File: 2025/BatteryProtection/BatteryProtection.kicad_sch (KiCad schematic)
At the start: 49 parts, among them J1 Conn_01x02_Socket, J2 Conn_01x02_Pin, J3 Conn_01x02_Pin, Q1 IXTA140P05T, Q10 BC847, Q11 BC847, Q12 BC847, Q2 BC847, Q3 BC847, Q4 BC847, Q5 BC847, Q6 BC847, Q7 BC847, Q8 BC847, Q9 BC847, U1 MCP6561-OT, U3 MCP6561-OT, U4 MCP1799x-330xxTT

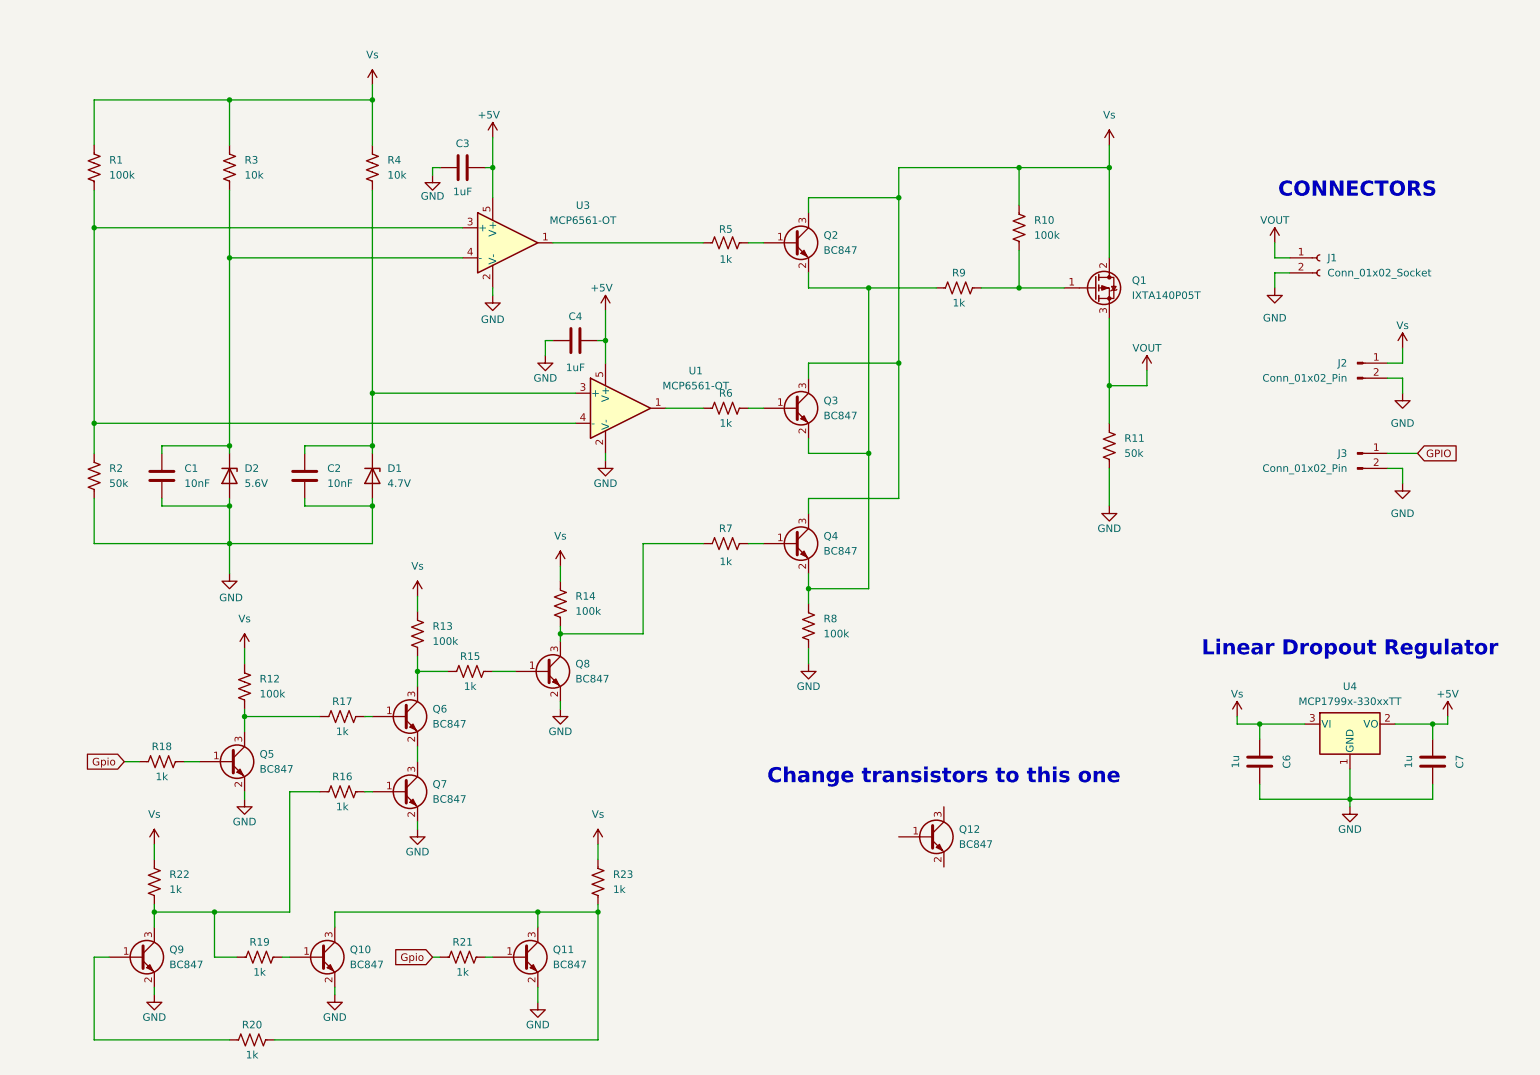
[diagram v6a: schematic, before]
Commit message: updated small bits in LTS and Kicad schematics
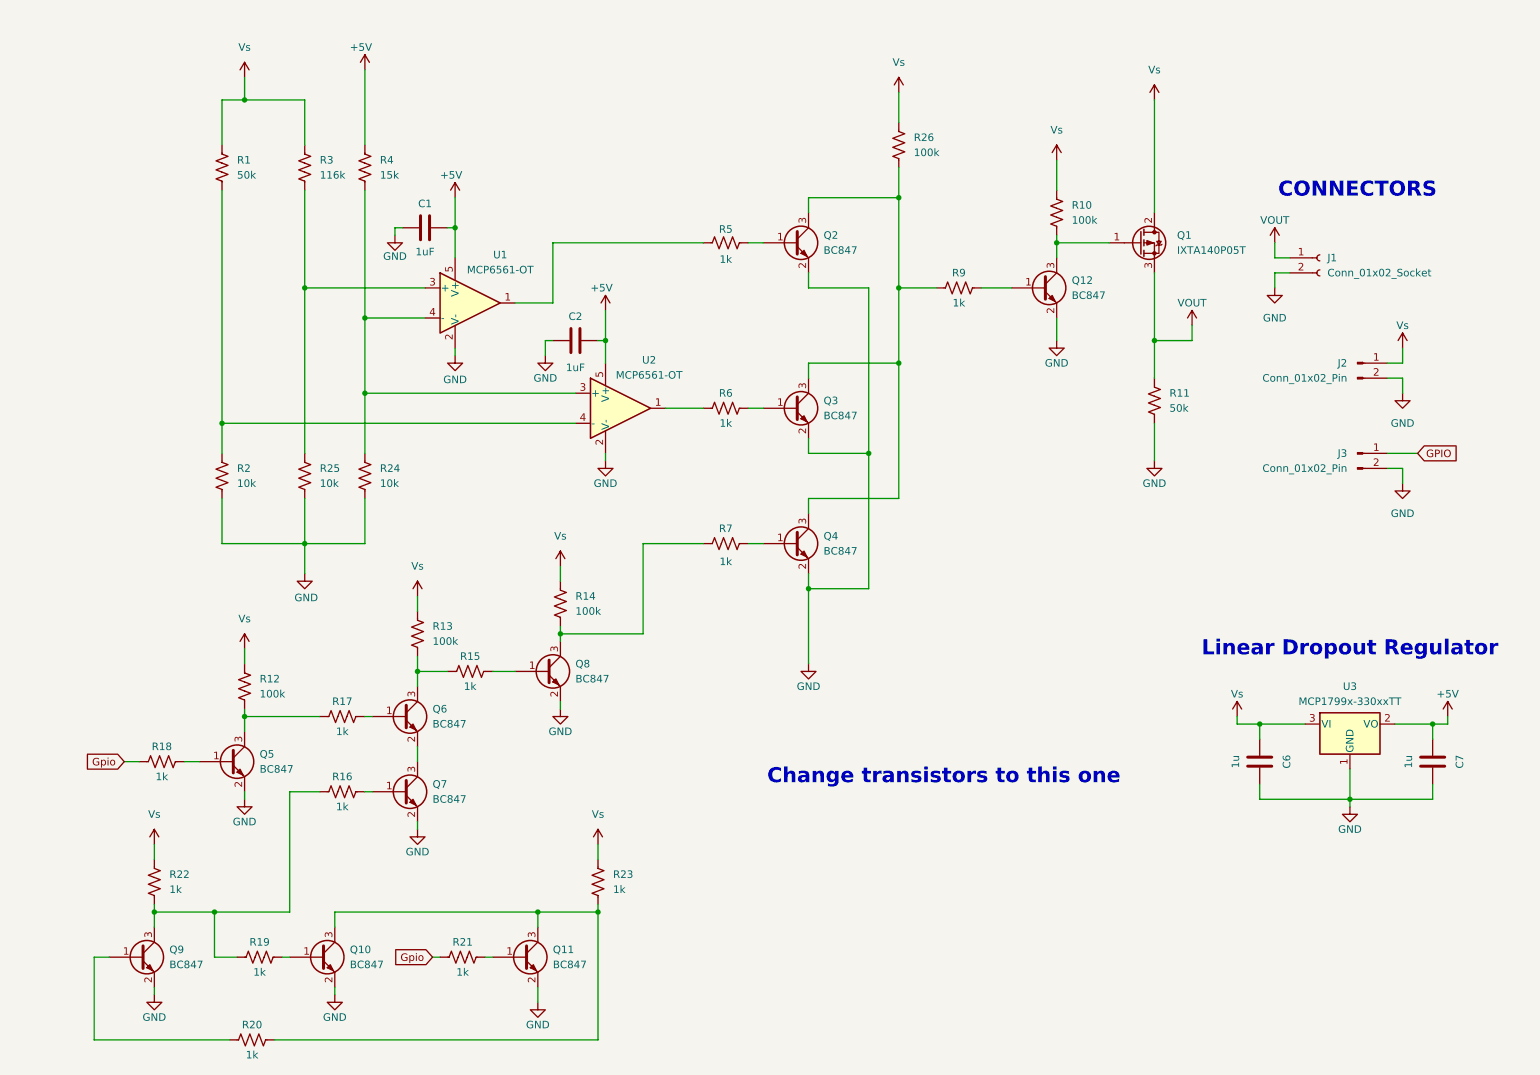
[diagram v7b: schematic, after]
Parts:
- removed C1, C2: 10nF, Capacitor_SMD:C_0603_1608Metric_Pad1.08x0.95mm_HandSolder, symbol Device:C
- removed D1: 4.7V, Diode_SMD:D_0603_1608Metric_Pad1.05x0.95mm_HandSolder, symbol Device:D_Zener
- removed D2: 5.6V, Diode_SMD:D_0603_1608Metric_Pad1.05x0.95mm_HandSolder, symbol Device:D_Zener
- removed R8: 100k, Resistor_SMD:R_0603_1608Metric_Pad0.98x0.95mm_HandSolder, symbol Device:R_US
- added R24, R25: 10k, Resistor_SMD:R_0603_1608Metric_Pad0.98x0.95mm_HandSolder, symbol Device:R_US
- added R26: 100k, Resistor_SMD:R_0603_1608Metric_Pad0.98x0.95mm_HandSolder, symbol Device:R_US
- R1: value 100k -> 50k
- R2: value 50k -> 10k
- R3: value 10k -> 116k
- R4: value 10k -> 15k
- renumbered C3 to C1, C4 to C2, U3 to U1, U1 to U2, U4 to U3
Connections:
- net +5V: now also R4.1
- net GND: now also Q12.2 (E), Q2.2 (E), Q3.2 (E), Q4.2 (E), R24.2, R25.2
- net Vs: now also R26.2; no longer Q2.3 (C), Q3.3 (C), Q4.3 (C), R4.1
- net at Q1.1 (G), R10.1: now also Q12.3 (C); no longer R9.1
- net at R4.2, U2.3 (+): now also U1.4 (-), R24.1
- net at R3.2: now also U1.3 (+), R25.1; no longer U1.4 (-)
- net at Q12.1 (B): now also R9.1
- net at R1.2, R2.1, U2.4 (-): no longer U1.3 (+)
- new net: Q2.3 (C), Q3.3 (C), Q4.3 (C), R26.1, R9.2
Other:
- moved on the sheet: C1, Q1, Q12, R1, R10, R11, R2, R3, R4, U1

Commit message: started PCB layout
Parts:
- renumbered C6 to C3, C7 to C4, R11 to R10, R12 to R11, R13 to R12, R14 to R13, R15 to R14, R18 to R15, R17 to R16, R16 to R17, R19 to R18, R20 to R19, R21 to R20, R22 to R21, R23 to R22, R24 to R23, R25 to R24, R26 to R25, R9 to R8, R10 to R9
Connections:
- net Gpio is gone; now on net GPIO: R15.1, R20.1
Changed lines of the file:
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@@
 		)
 	)
-	(global_label "Gpio"
+	(global_label "GPIO"
 		(shape input)
 		(at 44.45 142.24 180)
@@
 		)
 		(property "Intersheetrefs" "${INTERSHEET_REFS}"
-			(at 37.292 142.24 0)
+			(at 36.9895 142.24 0)
 			(effects
 				(font
@@
 		)
 	)
-	(global_label "Gpio"
+	(global_label "GPIO"
 		(shape input)
 		(at 96.52 175.26 180)
@@
 		)
 		(property "Intersheetrefs" "${INTERSHEET_REFS}"
-			(at 89.362 175.26 0)
+			(at 89.0595 175.26 0)
 			(effects
 				(font
@@
 		(dnp no)
 		(fields_autoplaced yes)
-		(property "Reference" "R22"
+		(property "Reference" "R21"
 			(at 52.07 161.2899 0)
 			(effects
@@
 			(project "BatteryProtection"
 				(path "/6c304649-7c80-4a4c-b925-07b9210ad53d"
-					(reference "R22")
+					(reference "R21")
 					(unit 1)
 				)
@@
 		(on_board yes)
 		(dnp no)
-		(property "Reference" "R19"
+		(property "Reference" "R18"
 			(at 67.31 172.72 90)
 			(effects
@@
 			(project "BatteryProtection"
 				(path "/6c304649-7c80-4a4c-b925-07b9210ad53d"
-					(reference "R19")
+					(reference "R18")
 					(unit 1)
 				)
@@
 		(dnp no)
 		(fields_autoplaced yes)
-		(property "Reference" "R12"
+		(property "Reference" "R11"
 			(at 67.31 128.2699 0)
 			(effects
@@
 			(project "BatteryProtection"
 				(path "/6c304649-7c80-4a4c-b925-07b9210ad53d"
-					(reference "R12")
+					(reference "R11")
 					(unit 1)
 				)
@@
 		(on_board yes)
 		(dnp no)
-		(property "Reference" "R21"
+		(property "Reference" "R20"
 			(at 101.6 172.72 90)
 			(effects
@@
 			(project "BatteryProtection"
 				(path "/6c304649-7c80-4a4c-b925-07b9210ad53d"
-					(reference "R21")
+					(reference "R20")
 					(unit 1)
 				)
@@
 		(dnp no)
 		(fields_autoplaced yes)
-		(property "Reference" "R10"
+		(property "Reference" "R9"
 			(at 204.47 48.2599 0)
 			(effects
@@
 			(project "BatteryProtection"
 				(path "/6c304649-7c80-4a4c-b925-07b9210ad53d"
-					(reference "R10")
+					(reference "R9")
 					(unit 1)
 				)
@@
 		(on_board yes)
 		(dnp no)
-		(property "Reference" "R20"
+		(property "Reference" "R19"
 			(at 66.04 186.69 90)
 			(effects
@@
 			(project "BatteryProtection"
 				(path "/6c304649-7c80-4a4c-b925-07b9210ad53d"
-					(reference "R20")
+					(reference "R19")
 					(unit 1)
 				)
@@
 		(dnp no)
 		(fields_autoplaced yes)
-		(property "Reference" "R26"
+		(property "Reference" "R25"
 			(at 177.8 36.8299 0)
 			(effects
@@
 			(project "BatteryProtection"
 				(path "/6c304649-7c80-4a4c-b925-07b9210ad53d"
-					(reference "R26")
+					(reference "R25")
 					(unit 1)
 				)
@@
 		(dnp no)
 		(fields_autoplaced yes)
-		(property "Reference" "R25"
+		(property "Reference" "R24"
 			(at 77.47 92.7099 0)
 			(effects
@@
 			(project "BatteryProtection"
 				(path "/6c304649-7c80-4a4c-b925-07b9210ad53d"
-					(reference "R25")
+					(reference "R24")
 					(unit 1)
 				)
@@
 		(dnp no)
 		(fields_autoplaced yes)
-		(property "Reference" "R24"
+		(property "Reference" "R23"
 			(at 87.63 92.7099 0)
 			(effects
@@
 			(project "BatteryProtection"
 				(path "/6c304649-7c80-4a4c-b925-07b9210ad53d"
-					(reference "R24")
+					(reference "R23")
 					(unit 1)
 				)
@@
 		(dnp no)
 		(fields_autoplaced yes)
-		(property "Reference" "R13"
+		(property "Reference" "R12"
 			(at 96.52 119.3799 0)
 			(effects
@@
 			(project "BatteryProtection"
 				(path "/6c304649-7c80-4a4c-b925-07b9210ad53d"
-					(reference "R13")
+					(reference "R12")
 					(unit 1)
 				)
@@
 		(on_board yes)
 		(dnp no)
-		(property "Reference" "C7"
+		(property "Reference" "C4"
 			(at 270.002 142.24 90)
 			(effects
@@
 			(project "BatteryProtection"
 				(path "/6c304649-7c80-4a4c-b925-07b9210ad53d"
-					(reference "C7")
+					(reference "C4")
 					(unit 1)
 				)
@@
 		(on_board yes)
 		(dnp no)
-		(property "Reference" "R9"
+		(property "Reference" "R8"
 			(at 185.42 59.69 90)
 			(effects
@@
 			(project "BatteryProtection"
 				(path "/6c304649-7c80-4a4c-b925-07b9210ad53d"
-					(reference "R9")
+					(reference "R8")
 					(unit 1)
 				)
@@
 		(on_board yes)
 		(dnp no)
-		(property "Reference" "R18"
+		(property "Reference" "R15"
 			(at 50.8 139.7 90)
 			(effects
@@
 			(project "BatteryProtection"
 				(path "/6c304649-7c80-4a4c-b925-07b9210ad53d"
-					(reference "R18")
+					(reference "R15")
 					(unit 1)
 				)
@@
 		(on_board yes)
 		(dnp no)
-		(property "Reference" "R17"
+		(property "Reference" "R16"
 			(at 81.28 132.08 90)
 			(effects
@@
 			(project "BatteryProtection"
 				(path "/6c304649-7c80-4a4c-b925-07b9210ad53d"
-					(reference "R17")
+					(reference "R16")
 					(unit 1)
 				)
@@
 		(on_board yes)
 		(dnp no)
-		(property "Reference" "R15"
+		(property "Reference" "R14"
 			(at 102.87 124.46 90)
 			(effects
@@
 			(project "BatteryProtection"
 				(path "/6c304649-7c80-4a4c-b925-07b9210ad53d"
-					(reference "R15")
+					(reference "R14")
 					(unit 1)
 				)
@@
 		(dnp no)
 		(fields_autoplaced yes)
-		(property "Reference" "R23"
+		(property "Reference" "R22"
 			(at 127 161.2899 0)
 			(effects
@@
 			(project "BatteryProtection"
 				(path "/6c304649-7c80-4a4c-b925-07b9210ad53d"
-					(reference "R23")
+					(reference "R22")
 					(unit 1)
 				)
@@
 		(on_board yes)
 		(dnp no)
-		(property "Reference" "C6"
+		(property "Reference" "C3"
 			(at 240.792 142.24 90)
 			(effects
@@
 			(project "BatteryProtection"
 				(path "/6c304649-7c80-4a4c-b925-07b9210ad53d"
-					(reference "C6")
+					(reference "C3")
 					(unit 1)
 				)
@@
 		(dnp no)
 		(fields_autoplaced yes)
-		(property "Reference" "R11"
+		(property "Reference" "R10"
 			(at 220.98 80.0099 0)
 			(effects
@@
 			(project "BatteryProtection"
 				(path "/6c304649-7c80-4a4c-b925-07b9210ad53d"
-					(reference "R11")
+					(reference "R10")
 					(unit 1)
 				)
@@
 		(on_board yes)
 		(dnp no)
-		(property "Reference" "R16"
+		(property "Reference" "R17"
 			(at 81.28 144.78 90)
 			(effects
@@
 			(project "BatteryProtection"
 				(path "/6c304649-7c80-4a4c-b925-07b9210ad53d"
-					(reference "R16")
+					(reference "R17")
 					(unit 1)
 				)
@@
 		(dnp no)
 		(fields_autoplaced yes)
-		(property "Reference" "R14"
+		(property "Reference" "R13"
 			(at 120.65 114.2999 0)
 			(effects
@@
 			(project "BatteryProtection"
 				(path "/6c304649-7c80-4a4c-b925-07b9210ad53d"
-					(reference "R14")
+					(reference "R13")
 					(unit 1)
 				)
